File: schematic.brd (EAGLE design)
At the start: 100 x 80 mm, 32 parts, among them Q3 IRF540, Q5 SPB80P06P

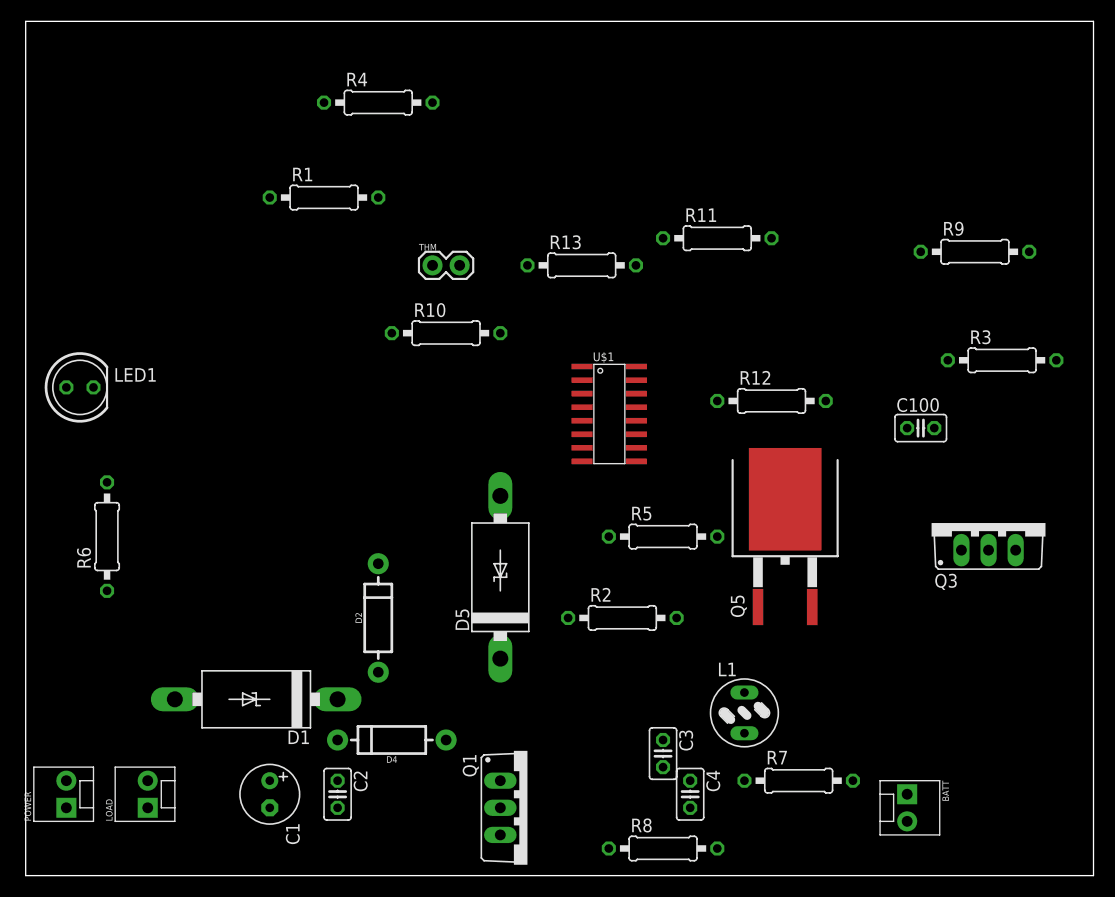
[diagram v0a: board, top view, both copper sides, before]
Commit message: Improve placement of elements
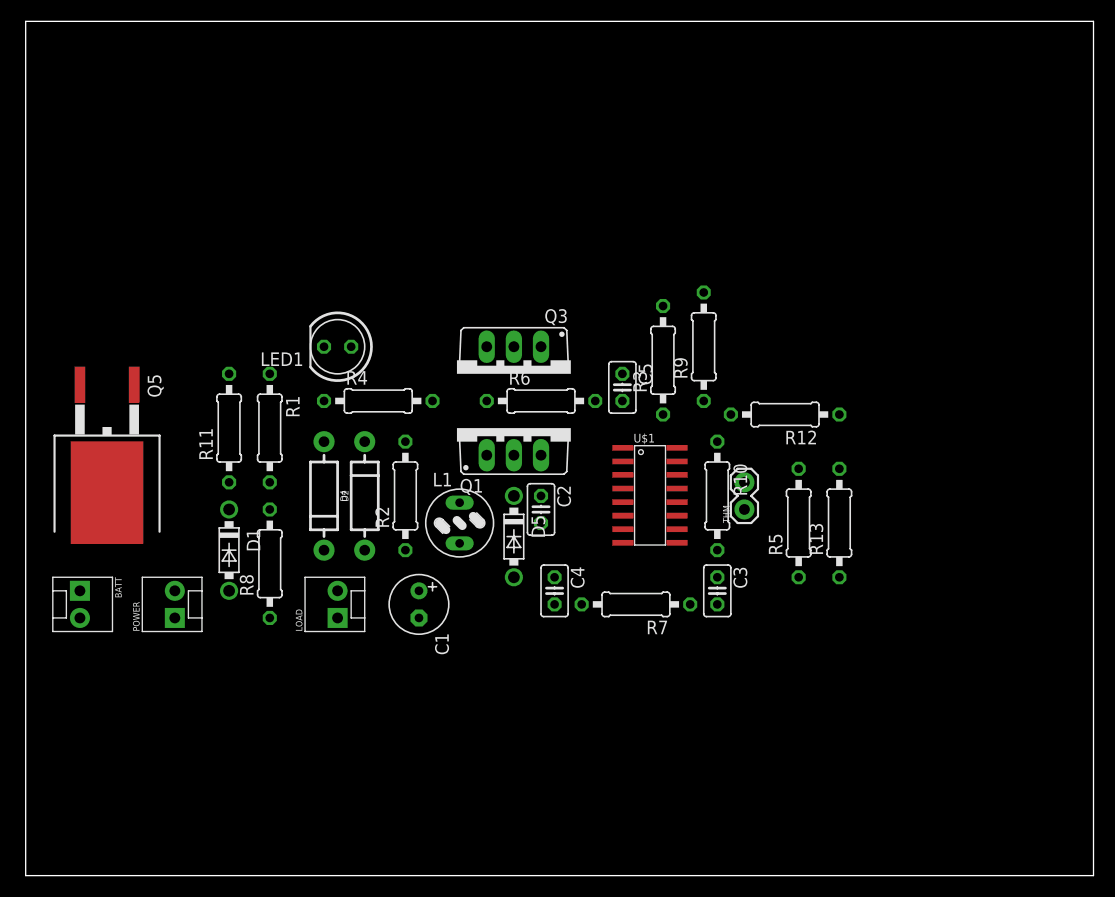
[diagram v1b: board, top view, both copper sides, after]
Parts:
- removed C100: (no value), rcl:C025-025X050
- added C5: (no value), rcl:C025-025X050
- D1, D5: value 1N5908 -> 1N5817-B; device diode:C4111-15 -> diode:DO41-7.6
- moved BATT 79.8 mm to (5.08, 26.7)
- moved Q5 64.0 mm to (7.62, 39.4), turned to 180 degrees
- moved R11 49.1 mm to (19.1, 41.9), turned to 90 degrees
- moved Q3 46.6 mm to (45.7, 47.0), turned to 180 degrees
- moved R8 45.5 mm to (22.9, 29.2), turned to 90 degrees
- moved R6 42.6 mm to (48.3, 44.5), turned to 0 degrees
- moved THM 37.1 mm to (67.3, 34.3), turned to 90 degrees
- moved Q1 35.6 mm to (45.7, 41.9), turned to 0 degrees
- moved R13 34.1 mm to (76.2, 33.0), turned to 90 degrees
- moved C2 32.8 mm to (48.3, 34.3)
- moved L1 32.1 mm to (40.6, 33.0)
- moved R3 31.8 mm to (59.7, 48.3), turned to 90 degrees
- moved R10 29.6 mm to (64.8, 35.6), turned to 270 degrees
- moved R4 27.9 mm to (33.0, 44.5)
- moved R9 26.9 mm to (63.5, 49.5), turned to 90 degrees
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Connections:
- net N$12: now also C5.2; no longer C100.2
- net N$14: now also C5.1; no longer C100.1
